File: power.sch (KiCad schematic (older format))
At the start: 23 parts, among them U3 LD3985M18R, U4 LM22676QMRX-5.0, U5 LD3985M33R

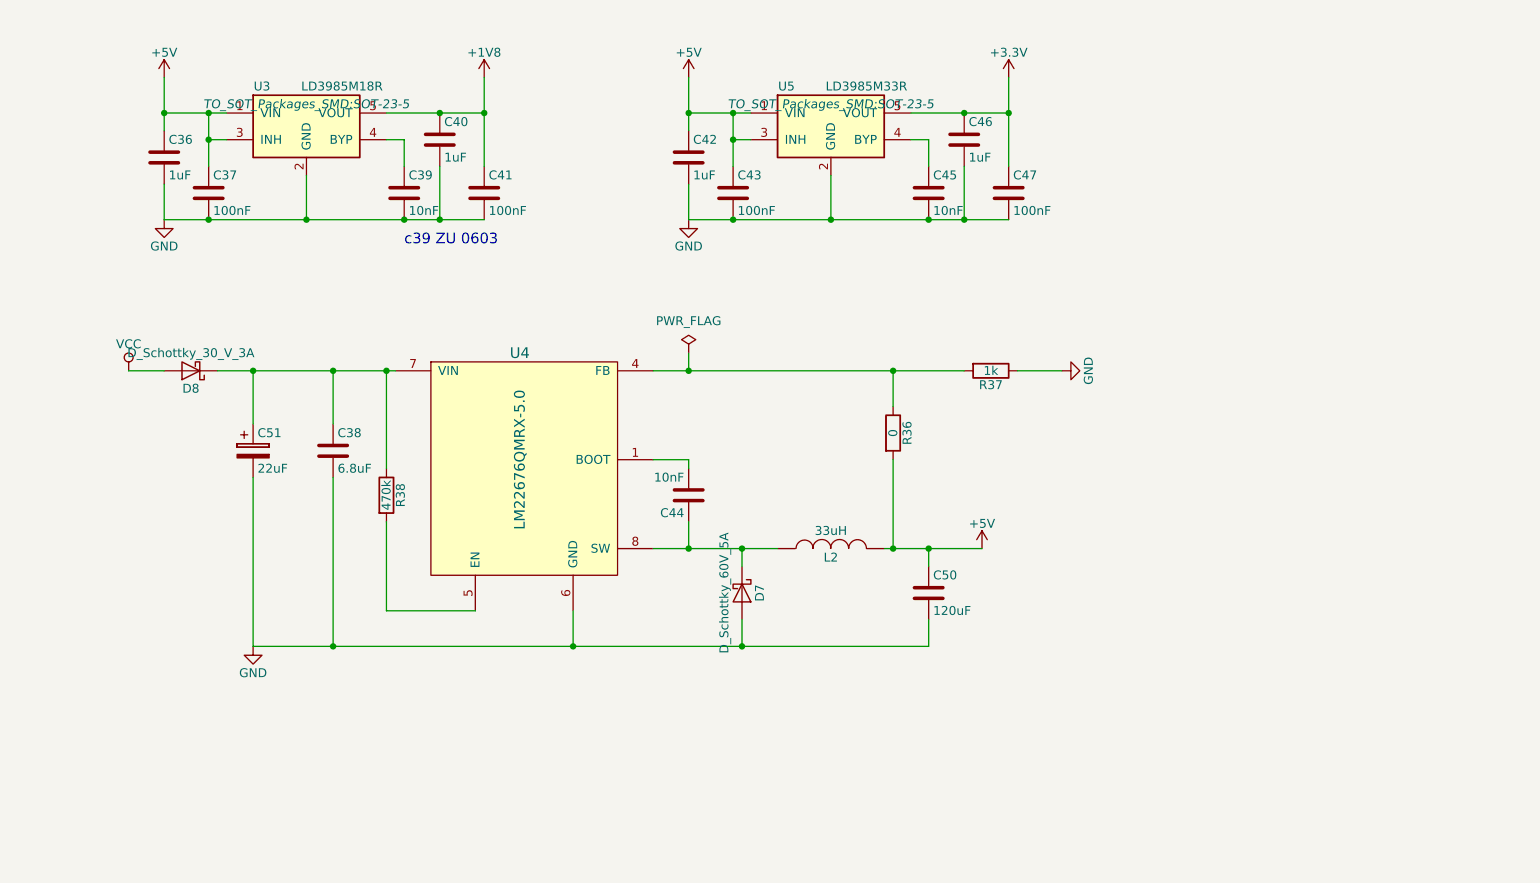
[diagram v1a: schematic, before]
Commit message: Use smd oscilator Add testpoints Use different power networks
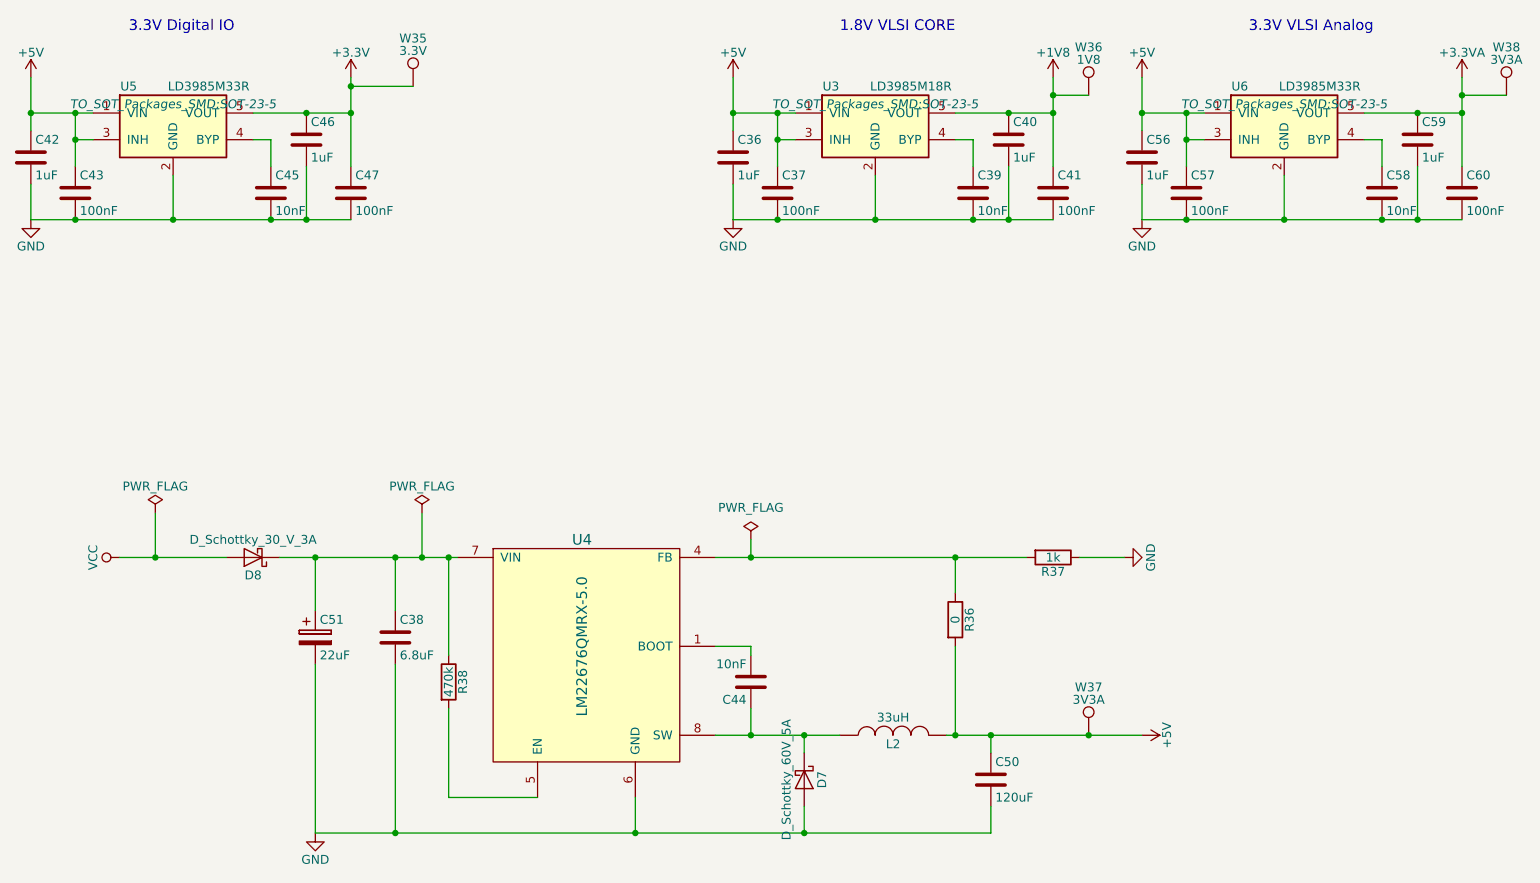
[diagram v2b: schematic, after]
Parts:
- added C56, C59: 1uF, Capacitors_SMD:C_0603, symbol C
- added C57, C60: 100nF, Capacitors_SMD:C_0402, symbol C
- added C58: 10nF, Capacitors_SMD:C_0603, symbol C
- added U6: LD3985M33R, TO_SOT_Packages_SMD:SOT-23-5, symbol LD3985M33R
- added W35: 3.3V, Measurement_Points:Measurement_Point_Round-SMD-Pad_Small, symbol TEST_1P
- added W36: 1V8, Measurement_Points:Measurement_Point_Round-SMD-Pad_Small, symbol TEST_1P
- added W37, W38: 3V3A, Measurement_Points:Measurement_Point_Round-SMD-Pad_Small, symbol TEST_1P
- C51: footprint Diodes_SMD:SMC_Standard -> jfi:SM2917_POL
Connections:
- net +1V8: now also W36.1
- net +3V3: now also W35.1
- net +5V: now also C56.1, C57.1, U6.1 (VIN), U6.3 (INH), W37.1
- net GND: now also C56.2, C57.2, C58.2, C59.2, C60.2, U6.2 (GND)
- new net: C58.1, U6.4 (BYP)
- new net +3.3VA: C59.1, C60.1, U6.5 (VOUT), W38.1
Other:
- note added: "1.8V VLSI CORE"
- note added: "3.3V Digital IO"
- note added: "3.3V VLSI Analog"
- note removed: "c39 ZU 0603"
- moved on the sheet: C36, C37, C38, C39, C40, C41, C42, C43, C44, C45, C46, C47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

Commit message: new layout
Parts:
- D8: footprint Diodes_SMD:SMB_Handsoldering -> Diodes_SMD:SMB_Standard
- R36: footprint Resistors_SMD:R_0805_HandSoldering -> Resistors_SMD:R_0603
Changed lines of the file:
@@
 F 0 "R36" V 7730 4200 50  0000 C CNN
 F 1 "0" V 7650 4200 50  0000 C CNN
-F 2 "Resistors_SMD:R_0805_HandSoldering" V 7580 4200 50  0001 C CNN
+F 2 "Resistors_SMD:R_0603" V 7580 4200 50  0001 C CNN
 F 3 "" H 7650 4200 50  0001 C CNN
 F 4 "" H 350 1050 50  0001 C CNN "MFR"
@@
 F 0 "D8" H 3700 3950 50  0000 C CNN
 F 1 "D_Schottky_30_V_3A" H 3700 3750 50  0000 C CNN
-F 2 "Diodes_SMD:SMB_Handsoldering" H 3700 3850 50  0001 C CNN
+F 2 "Diodes_SMD:SMB_Standard" H 3700 3850 50  0001 C CNN
 F 3 "" H 3700 3850 50  0001 C CNN
 F 4 "Mouser" H 3700 3850 60  0001 C CNN "SPR"

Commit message: Finished new layout
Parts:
- C36: MFR (none) -> AVX; MPN (none) -> TAJA105K016RNJ; SPN 581-0603YD105K -> 581-TAJA105K016
- C38: MPN C1608X5R1C685K080AB -> C1608X5R1E685K080AC; SPN 810-C1608X5R1C685K0B -> 810-C1608X5R1E685KAC
- C40, C42, C46, C56, C59: MFR (none) -> AVX; MPN (none) -> TAJA105K016RNJ; SPN (none) -> 581-TAJA105K016; SPR (none) -> Mouser
- R36: MFR (none) -> YAGEO; MPN (none) -> RC0603JR-070RL; SPN (none) -> 603-RC0603JR-070RL; SPR (none) -> Mouser

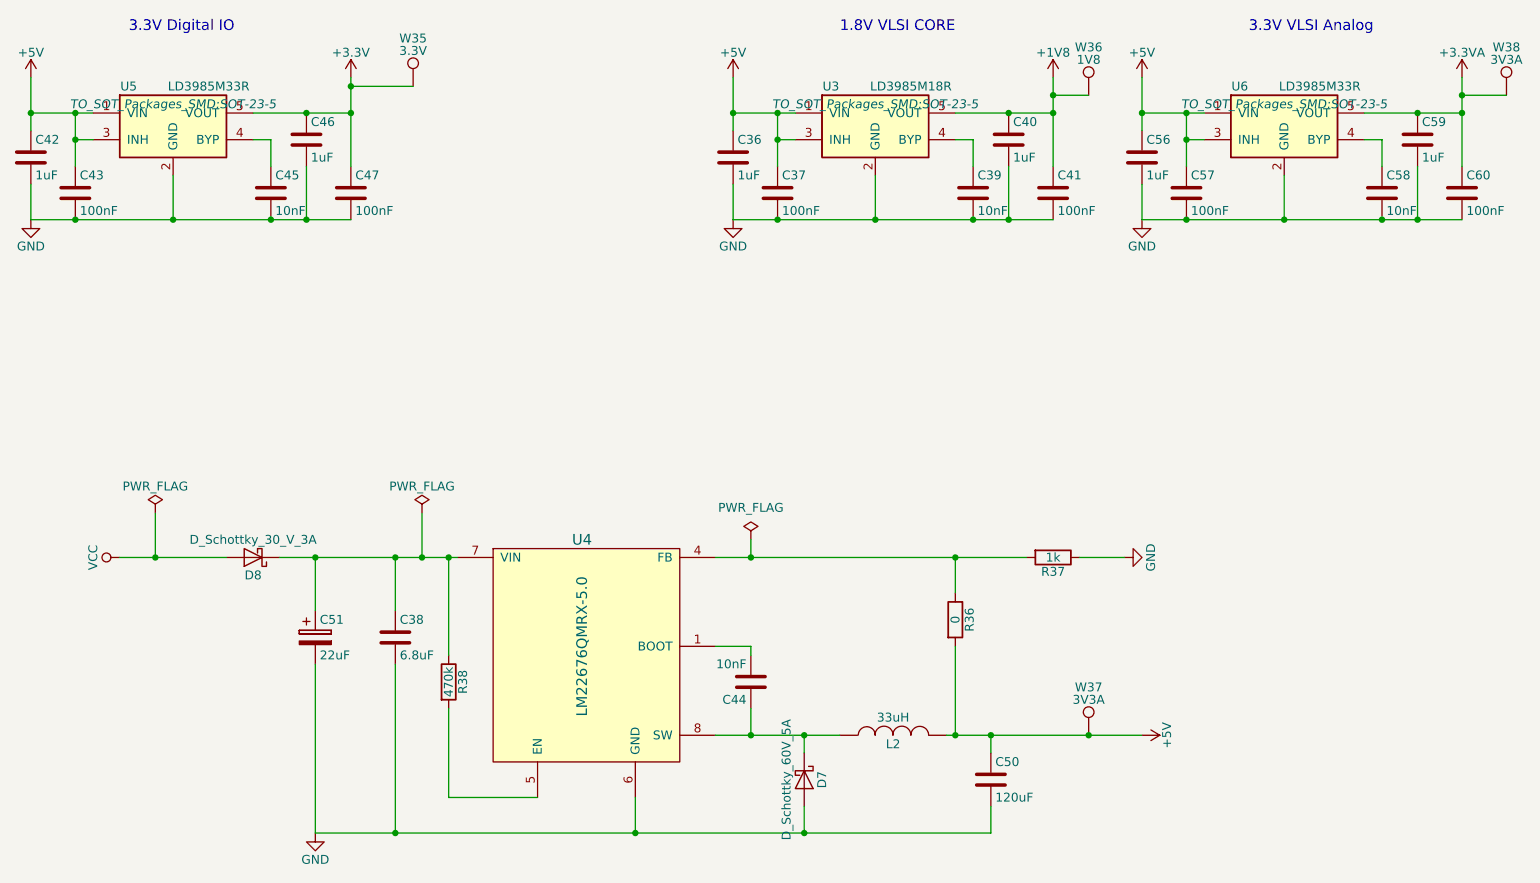
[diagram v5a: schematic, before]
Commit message: Remove 3. LDO some improvements
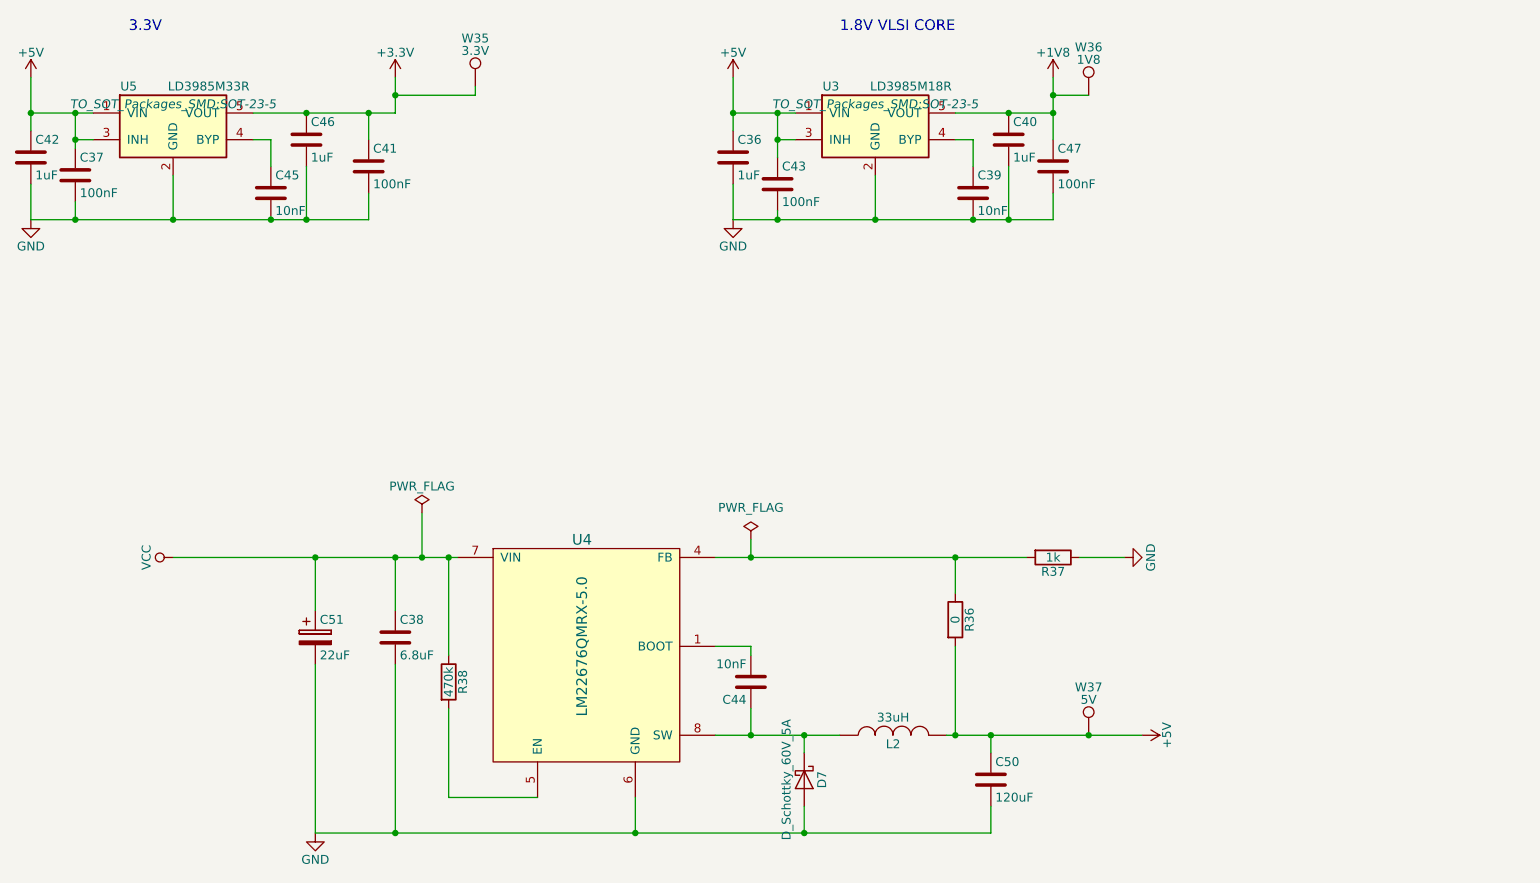
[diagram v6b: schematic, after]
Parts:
- removed C56, C59: 1uF, Capacitors_SMD:C_0603, symbol C
- removed C57, C60: 100nF, Capacitors_SMD:C_0402, symbol C
- removed C58: 10nF, Capacitors_SMD:C_0603, symbol C
- removed D8: D_Schottky_30_V_3A, Diodes_SMD:SMB_Standard, symbol D_Schottky
- removed U6: LD3985M33R, TO_SOT_Packages_SMD:SOT-23-5, symbol LD3985M33R
- removed W38: 3V3A, Measurement_Points:Measurement_Point_Round-SMD-Pad_Small, symbol TEST_1P
- W37: value 3V3A -> 5V
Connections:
- net +1V8: now also C47.1; no longer C41.1
- net +3V3: now also C41.1; no longer C47.1
- net VCC: now also C38.1, C51.1, R38.1, U4.7 (VIN)
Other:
- note added: "3.3V"
- note removed: "3.3V Digital IO"
- note removed: "3.3V VLSI Analog"
- moved on the sheet: W35
